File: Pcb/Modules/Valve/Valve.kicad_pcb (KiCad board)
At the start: 2 copper layers, 53.3 x 45.7 mm, 19 parts, among them CON1 Valve1, CON2 Valve3, CON3 Power, CON4 Valve2, CON5 Valve4, J1 JACK_RJ45, P1 Servo1, P2 Servo2, Q1 Q_NMOS_GSD, Q2 Q_NMOS_GSD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

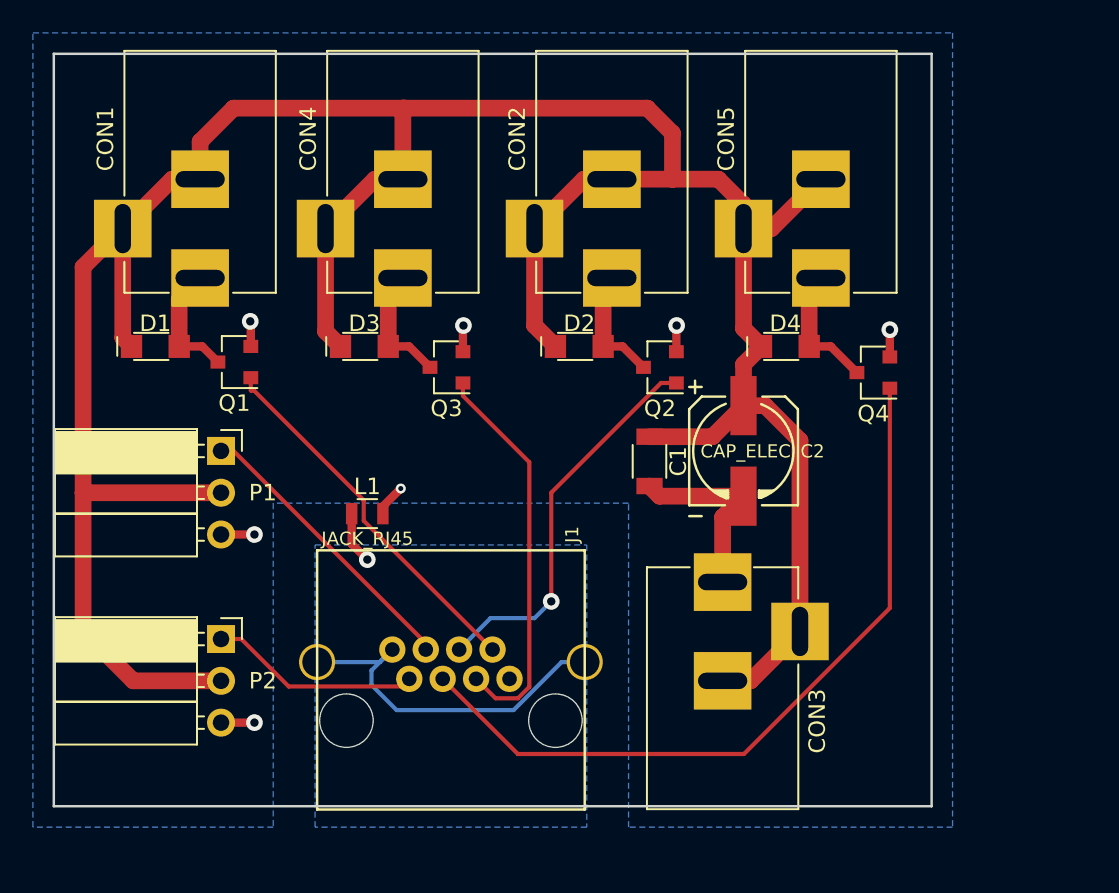
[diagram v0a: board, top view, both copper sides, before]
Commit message: Update module pcbs to common format and fix issues.
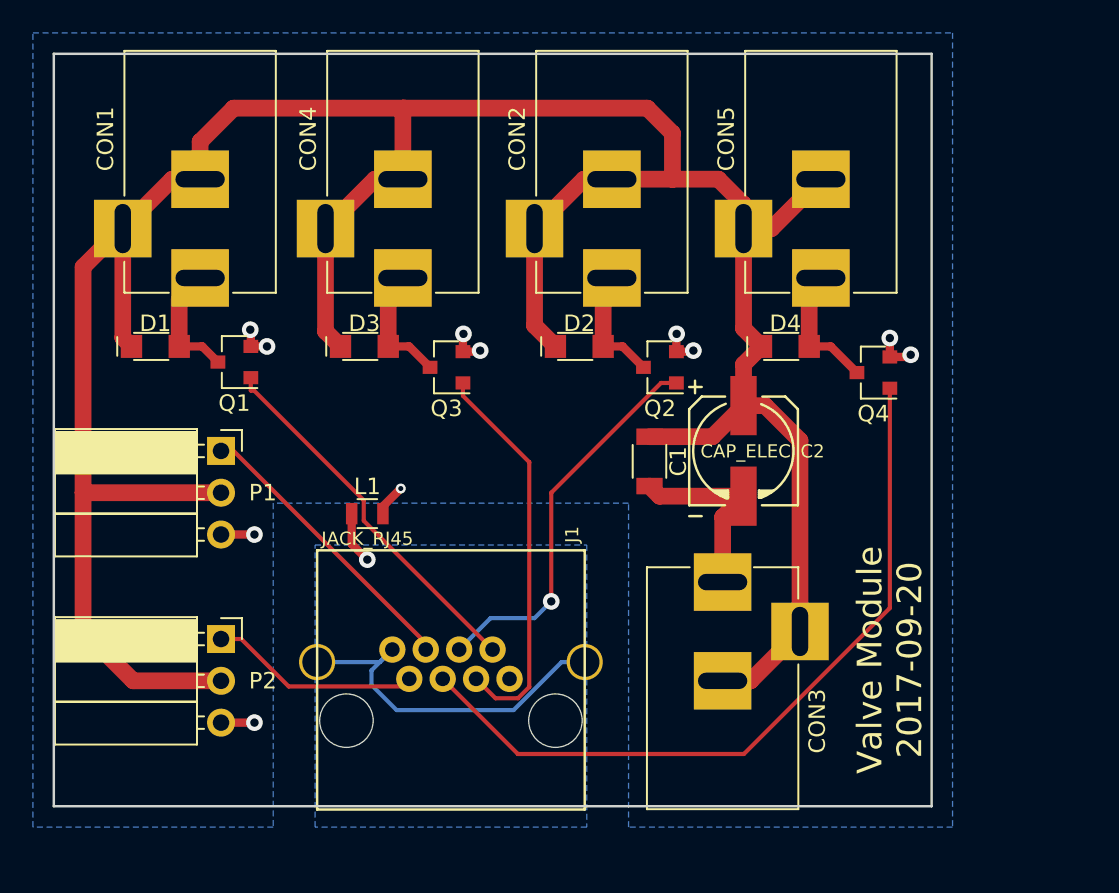
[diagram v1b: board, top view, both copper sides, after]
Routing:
- net GND: track 24.1 -> 26.6 mm, vias 7 -> 11
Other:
- board text added: "Valve Module 2017-09-20"

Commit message: Update Valve module
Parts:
- removed CON1: Valve1, Connectors:BARREL_JACK
- removed CON2: Valve3, Connectors:BARREL_JACK
- removed CON3: Power, Connectors:BARREL_JACK
- removed CON4: Valve2, Connectors:BARREL_JACK
- removed CON5: Valve4, Connectors:BARREL_JACK
- added D5: LED, LEDs:LED_0805, F.Cu at (78.7, 69.8)
- added POWER1: Power, Connectors:BARREL_JACK, F.Cu at (69.8, 57.4)
- added R1: 1K, Resistors_SMD:R_0603, F.Cu at (42.9, 46.2)
- added R2: 10K, Resistors_SMD:R_0603, F.Cu at (42.9, 43.7)
- added R3: 1K, Resistors_SMD:R_0603, F.Cu at (55.4, 46.5)
- added R4: 10K, Resistors_SMD:R_0603, F.Cu at (55.4, 43.9)
- added R5: 1K, Resistors_SMD:R_0603, F.Cu at (68.8, 46.5)
- added R6: 10K, Resistors_SMD:R_0603, F.Cu at (68.8, 43.9)
- added R7: 1K, Resistors_SMD:R_0603, F.Cu at (81.8, 46.7)
- added R8: 10K, Resistors_SMD:R_0603, F.Cu at (81.8, 44.2)
- added R9: 1K, Resistors_SMD:R_0603, F.Cu at (78.7, 67.8)
- added Valve1: Valve1, Connectors:BARREL_JACK, F.Cu at (38.1, 39.1)
- added Valve2: Valve2, Connectors:BARREL_JACK, F.Cu at (50.5, 39.1)
- added Valve3: Valve3, Connectors:BARREL_JACK, F.Cu at (63.0, 39.1)
- added Valve4: Valve4, Connectors:BARREL_JACK, F.Cu at (75.9, 39.1)
- added X1: HOLE, Mounting_Holes:MountingHole_2.2mm_M2_ISO14580_Pad, F.Cu at (27.9, 27.9)
- added X2: HOLE, Mounting_Holes:MountingHole_2.2mm_M2_ISO14580_Pad, F.Cu at (83.8, 27.9)
- added X3: HOLE, Mounting_Holes:MountingHole_2.2mm_M2_ISO14580_Pad, F.Cu at (27.9, 68.6)
- added X4: HOLE, Mounting_Holes:MountingHole_2.2mm_M2_ISO14580_Pad, F.Cu at (83.8, 68.6)
- C1: value C -> 10uF
- C2: value CAP_ELEC -> 100uF
- moved Q3 16.8 mm to (66.0, 44.5)
- moved Q2 9.65 mm to (52.6, 44.5)
- moved C2 5.74 mm to (72.8, 51.1), turned to 180 degrees
- moved D2 3.88 mm to (61.2, 43.2)
- moved C1 3.81 mm to (65.4, 50.2)
- moved D1 3.81 mm to (35.4, 43.2)
- moved D4 3.81 mm to (73.7, 43.2)
- moved J1 3.81 mm to (53.3, 63.5)
- moved Q1 3.81 mm to (40.2, 44.1)
- moved Q4 3.81 mm to (79.0, 44.8)
- moved D3 3.74 mm to (48.0, 43.2)
- moved L1 3.06 mm to (47.5, 53.1), turned to 180 degrees
- moved Servo2 2.03 mm to (35.6, 58.9)
- moved Servo1 0.51 mm to (35.6, 49.0)
- renumbered P1 to Servo1, P2 to Servo2
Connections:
- D2 pad 2: Net-(CON2-Pad1) -> Net-(D2-Pad2)
- D3 pad 2: Net-(CON4-Pad1) -> Net-(D3-Pad2)
- Q1 pad 1: /Valve1 -> Net-(Q1-Pad1)
- Q2 pad 1: /Valve3 -> Net-(Q2-Pad1)
- Q2 pad 3: Net-(CON2-Pad1) -> Net-(D3-Pad2)
- Q3 pad 1: /Valve2 -> Net-(Q3-Pad1)
- Q3 pad 3: Net-(CON4-Pad1) -> Net-(D2-Pad2)
- Q4 pad 1: /Valve4 -> Net-(Q4-Pad1)
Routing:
- net +12V: track 179.7 -> 132.3 mm
- net Net-(D3-Pad2): track 0.00 -> 16.7 mm
- net Net-(D2-Pad2): track 0.00 -> 16.7 mm
- net Net-(D4-Pad2): track 8.01 -> 17.8 mm
- net Net-(D1-Pad2): track 7.43 -> 17.0 mm
- net GND: track 26.6 -> 17.5 mm, vias 11 -> 13
- net /Servo1: track 17.8 -> 25.9 mm, vias 0 -> 1
- net Net-(CON4-Pad1): track 7.59 -> 0.00 mm
- net Net-(CON2-Pad1): track 7.36 -> 0.00 mm
- net Net-(J1-Pad8): track 25.5 -> 32.4 mm, vias 1 -> 0
- net /Servo2: track 12.8 -> 17.3 mm, vias 0 -> 1
- net Net-(Q2-Pad1): track 0.00 -> 2.97 mm
- net Net-(Q3-Pad1): track 0.00 -> 2.97 mm
- net Net-(Q1-Pad1): track 0.00 -> 2.95 mm
- net Net-(Q4-Pad1): track 0.00 -> 2.93 mm
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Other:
- board size 53.3 x 45.7 mm -> 61 x 45.7 mm
- rule trace_min: 0.2 -> 0.1524
- board text added: "Valve Module 2017-10-11"
- board text removed: "Valve Module 2017-09-20"

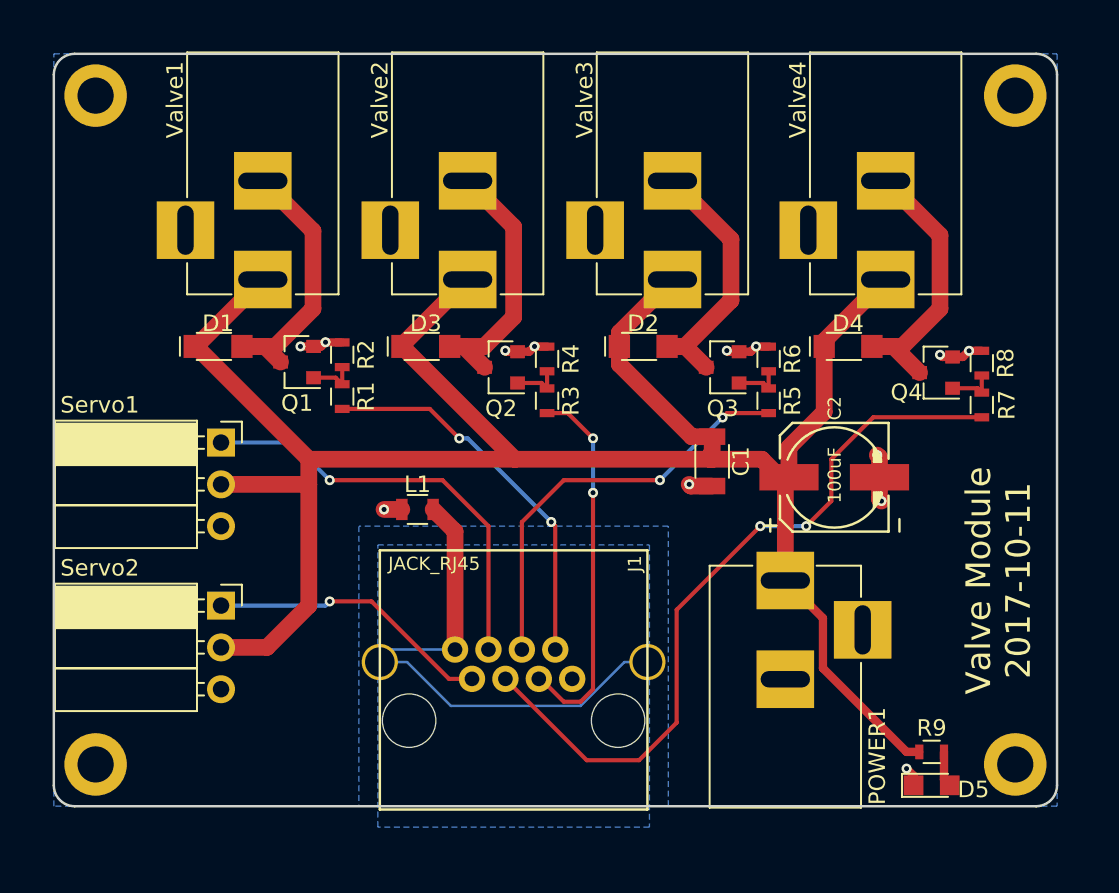
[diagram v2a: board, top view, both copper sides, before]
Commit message: Fix up PCB traces
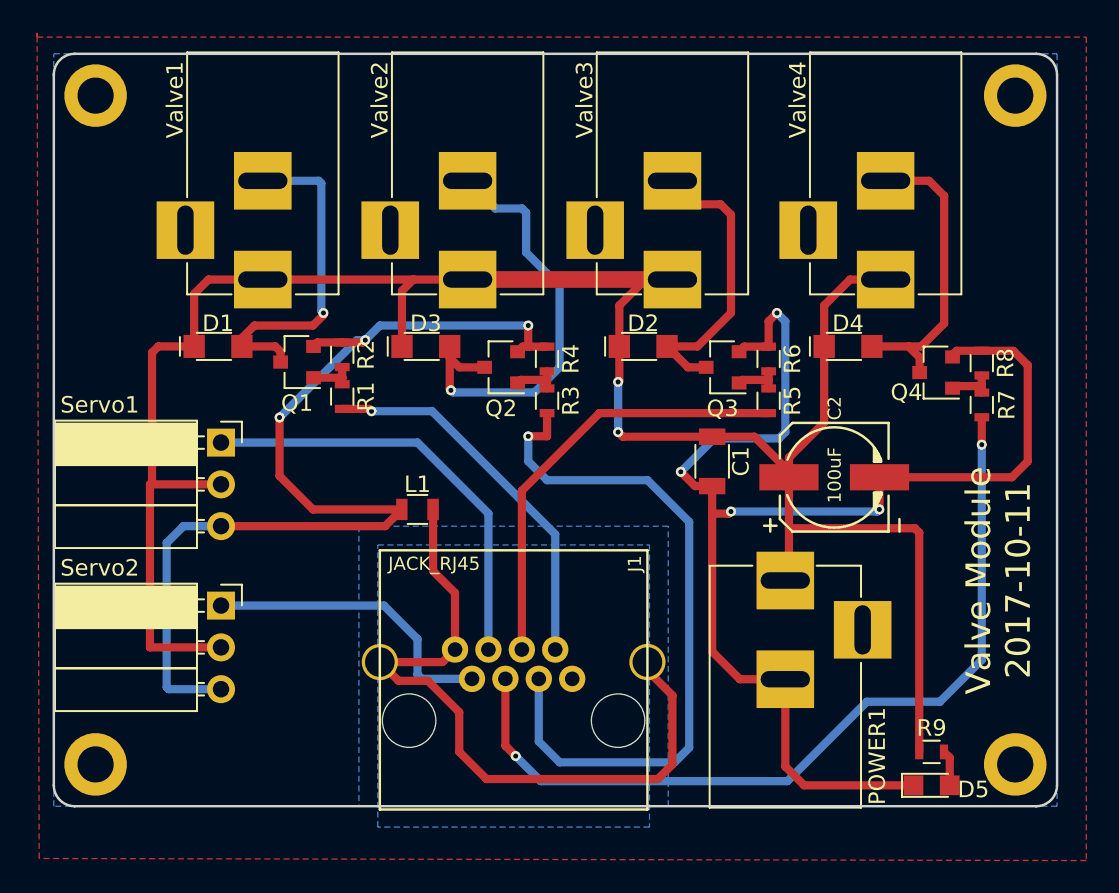
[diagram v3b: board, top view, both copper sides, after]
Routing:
- net GND: track 17.5 -> 145.7 mm, vias 13 -> 7
- net /Valve2: track 22.9 -> 42.9 mm, vias 2 -> 1
- net Net-(D3-Pad2): track 16.7 -> 27.6 mm, vias 0 -> 1
- net Net-(J1-Pad8): track 32.4 -> 43.3 mm
- net /Valve4: track 45.1 -> 51.7 mm
- net Net-(D1-Pad2): track 17.0 -> 20.8 mm, vias 0 -> 1
- net Net-(D2-Pad2): track 16.7 -> 18.0 mm
- net /Valve3: track 25.5 -> 26.6 mm, vias 2 -> 0
- net /Servo2: track 17.3 -> 18.4 mm, vias 1 -> 0
- net +12V: track 132.3 -> 133.0 mm, vias 0 -> 2
- net Net-(D4-Pad2): track 17.8 -> 18.5 mm
- net /Servo1: track 25.9 -> 26.3 mm, vias 1 -> 0
- net /Valve1: track 23.4 -> 23.1 mm, vias 2 -> 1
- added copper zone on F.Cu, net GND
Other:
- net class Default: trace_width 0.254 -> 0.5

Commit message: Update PCBs
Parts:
- removed L1: Ferrite_Bead, Resistors_SMD:R_0805
- X1, X2, X3, X4: footprint Mounting_Holes:MountingHole_2.2mm_M2_ISO14580_Pad -> Mounting_Holes:MountingHole_2.5mm_Pad
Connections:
- J1 pad 8: Net-(J1-Pad8) -> GND
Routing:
- net GND: track 145.7 -> 24.0 mm, vias 7 -> 10
- net Net-(J1-Pad8): track 43.3 -> 0.00 mm
- net +12V: track 133.0 -> 157.4 mm, vias 2 -> 3
- net /Valve2: track 42.9 -> 41.0 mm, vias 1 -> 2
- net /Servo2: track 18.4 -> 17.7 mm
- removed copper zone on F.Cu, net GND
- removed copper zone on B.Cu, net Net-(J1-Pad8)
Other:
- board text added: "Valve Module 2017-12-03"
- board text removed: "Valve Module 2017-10-11"

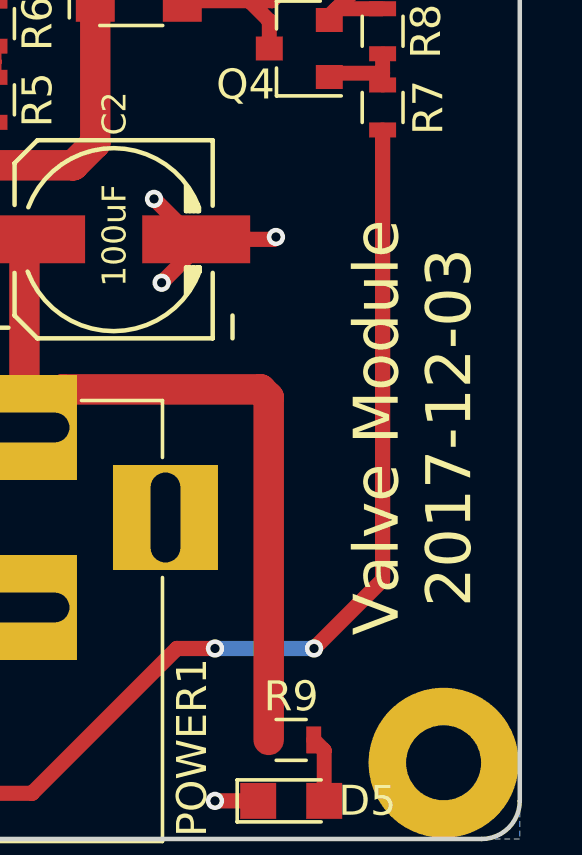
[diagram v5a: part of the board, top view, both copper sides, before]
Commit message: Update CA6 PCB.  Also update versions of all the module pcbs to match.
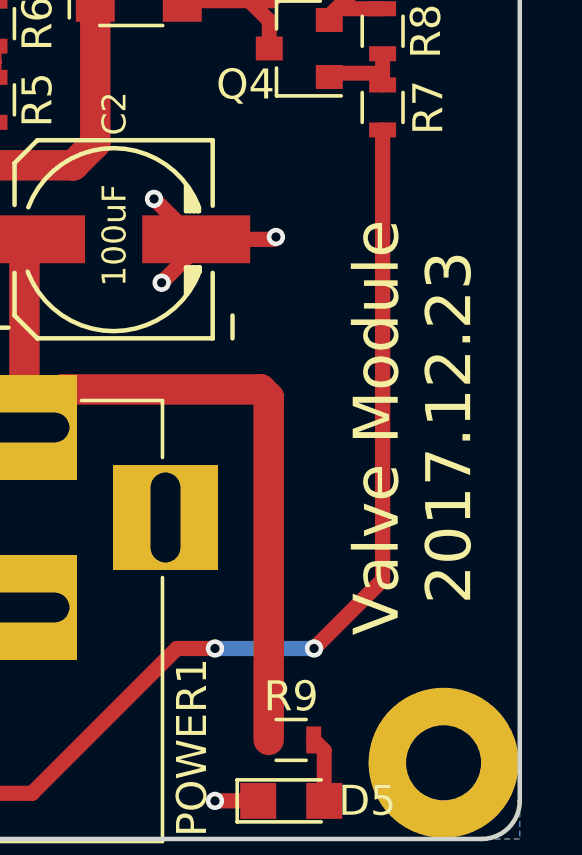
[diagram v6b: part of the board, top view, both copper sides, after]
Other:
- board text added: "Valve Module 2017.12.23"
- board text removed: "Valve Module 2017-12-03"
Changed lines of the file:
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@@
   (gr_arc (start 26.67 26.67) (end 25.4 26.67) (angle 90) (layer Edge.Cuts) (width 0.15))
   (gr_arc (start 26.67 69.85) (end 26.67 71.12) (angle 90) (layer Edge.Cuts) (width 0.15))
-  (gr_text "Valve Module\n2017-12-03" (at 82.804 57.404 90) (layer F.SilkS)
+  (gr_text "Valve Module\n2017.12.23" (at 82.804 57.404 90) (layer F.SilkS)
     (effects (font (size 1.5 1.5) (thickness 0.3)))
   )

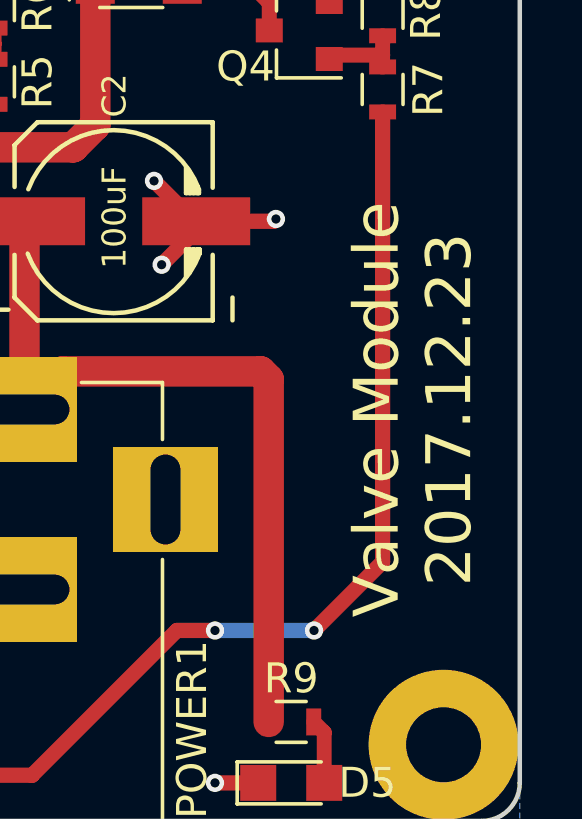
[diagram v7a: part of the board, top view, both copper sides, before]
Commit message: Move holes on sound module to match other modules.  Updated silkscreens on other modules.  Generate gerbers
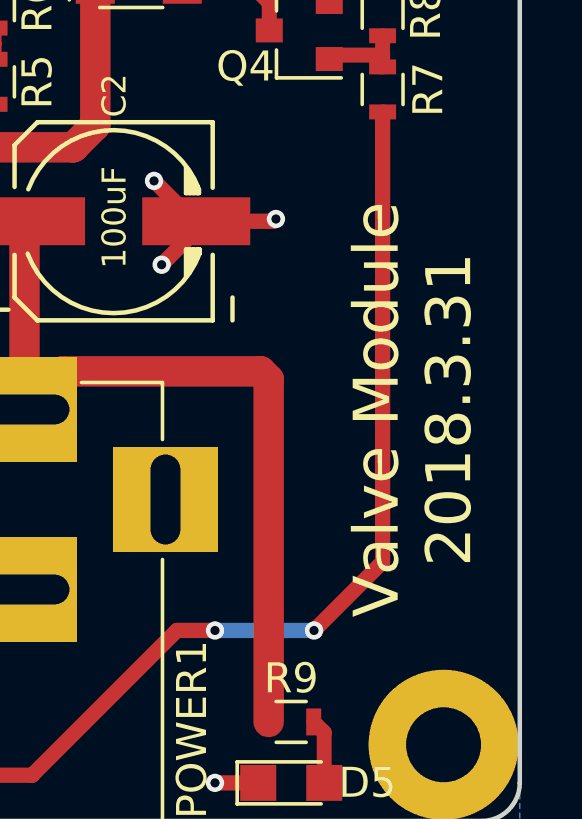
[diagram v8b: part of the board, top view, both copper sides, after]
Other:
- board text added: "Valve Module 2018.3.31"
- board text removed: "Valve Module 2017.12.23"
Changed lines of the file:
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@@
   (gr_arc (start 26.67 26.67) (end 25.4 26.67) (angle 90) (layer Edge.Cuts) (width 0.15))
   (gr_arc (start 26.67 69.85) (end 26.67 71.12) (angle 90) (layer Edge.Cuts) (width 0.15))
-  (gr_text "Valve Module\n2017.12.23" (at 82.804 57.404 90) (layer F.SilkS)
+  (gr_text "Valve Module\n2018.3.31" (at 82.804 57.404 90) (layer F.SilkS)
     (effects (font (size 1.5 1.5) (thickness 0.3)))
   )
